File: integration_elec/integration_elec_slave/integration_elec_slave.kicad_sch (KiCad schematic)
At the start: 0 parts

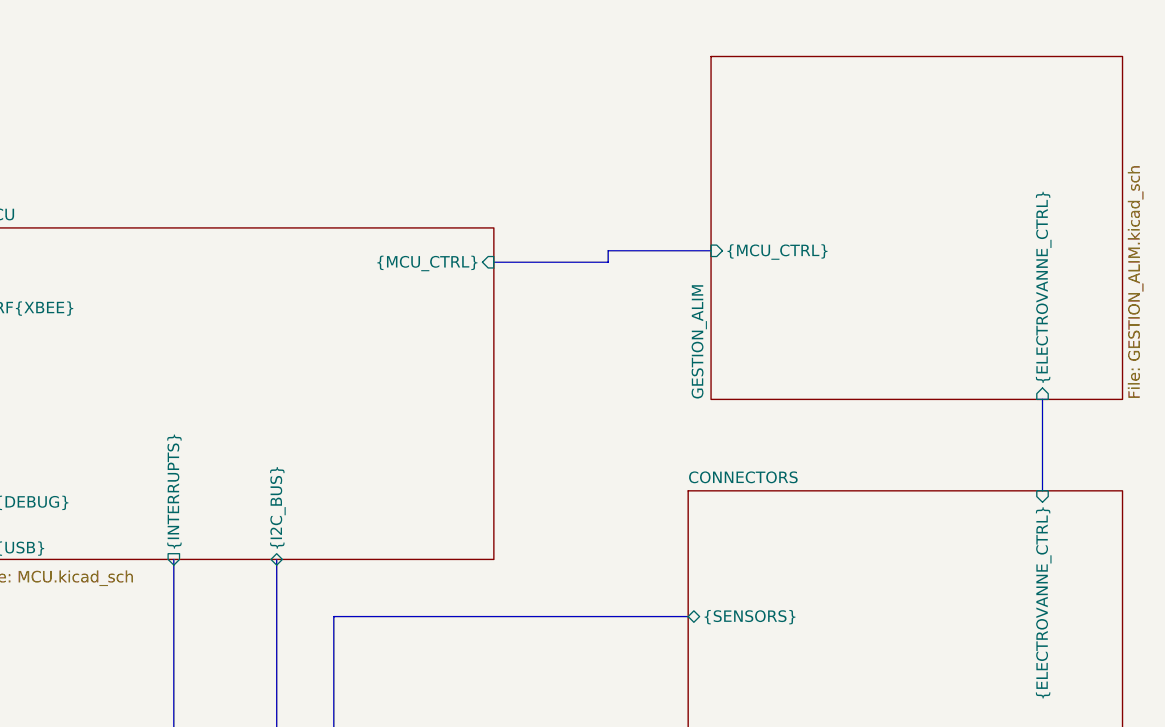
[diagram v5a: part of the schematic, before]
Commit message: EM - Fini schématique attente de review
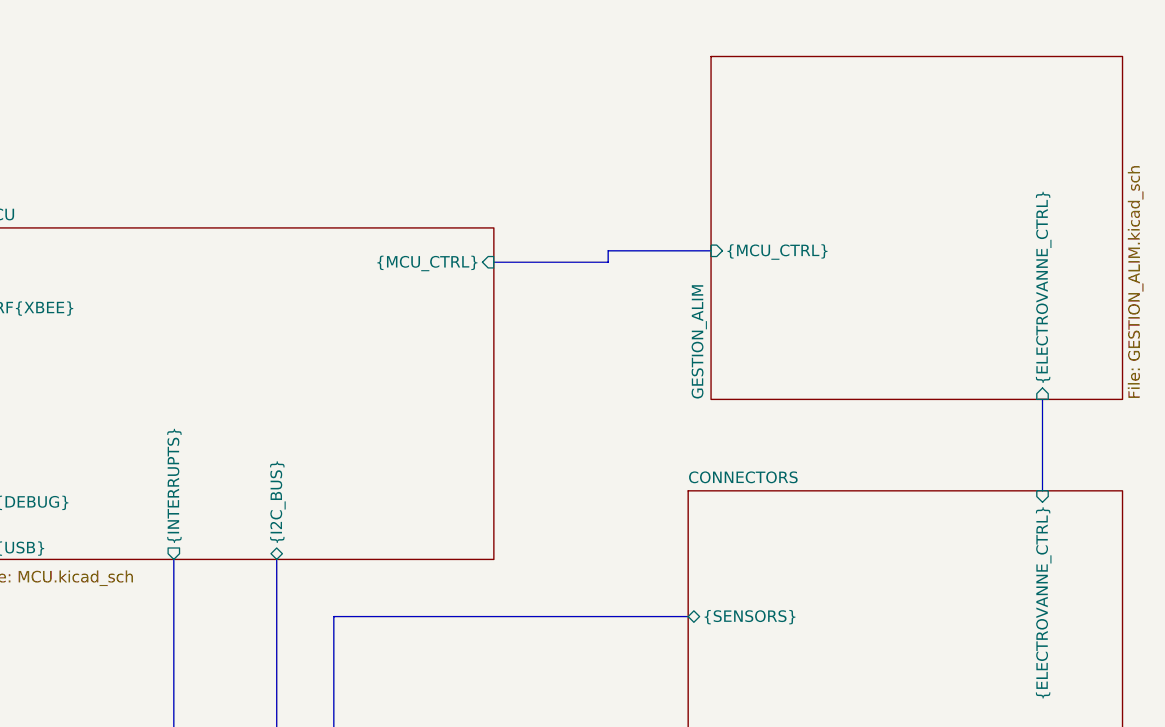
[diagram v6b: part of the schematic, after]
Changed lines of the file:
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@@
 		)
 		(pin "{ELECTROVANNE_CTRL}" input
-			(at 257.8101 81.2799 270)
+			(at 257.8101 81.28 270)
 			(effects
 				(font
@@
 		)
 		(pin "{I2C_BUS}" bidirectional
-			(at 172.72 99.695 270)
+			(at 172.72 99.06 270)
 			(effects
 				(font
@@
 		)
 		(pin "{INTERRUPTS}" output
-			(at 161.29 99.695 270)
+			(at 161.29 99.06 270)
 			(effects
 				(font

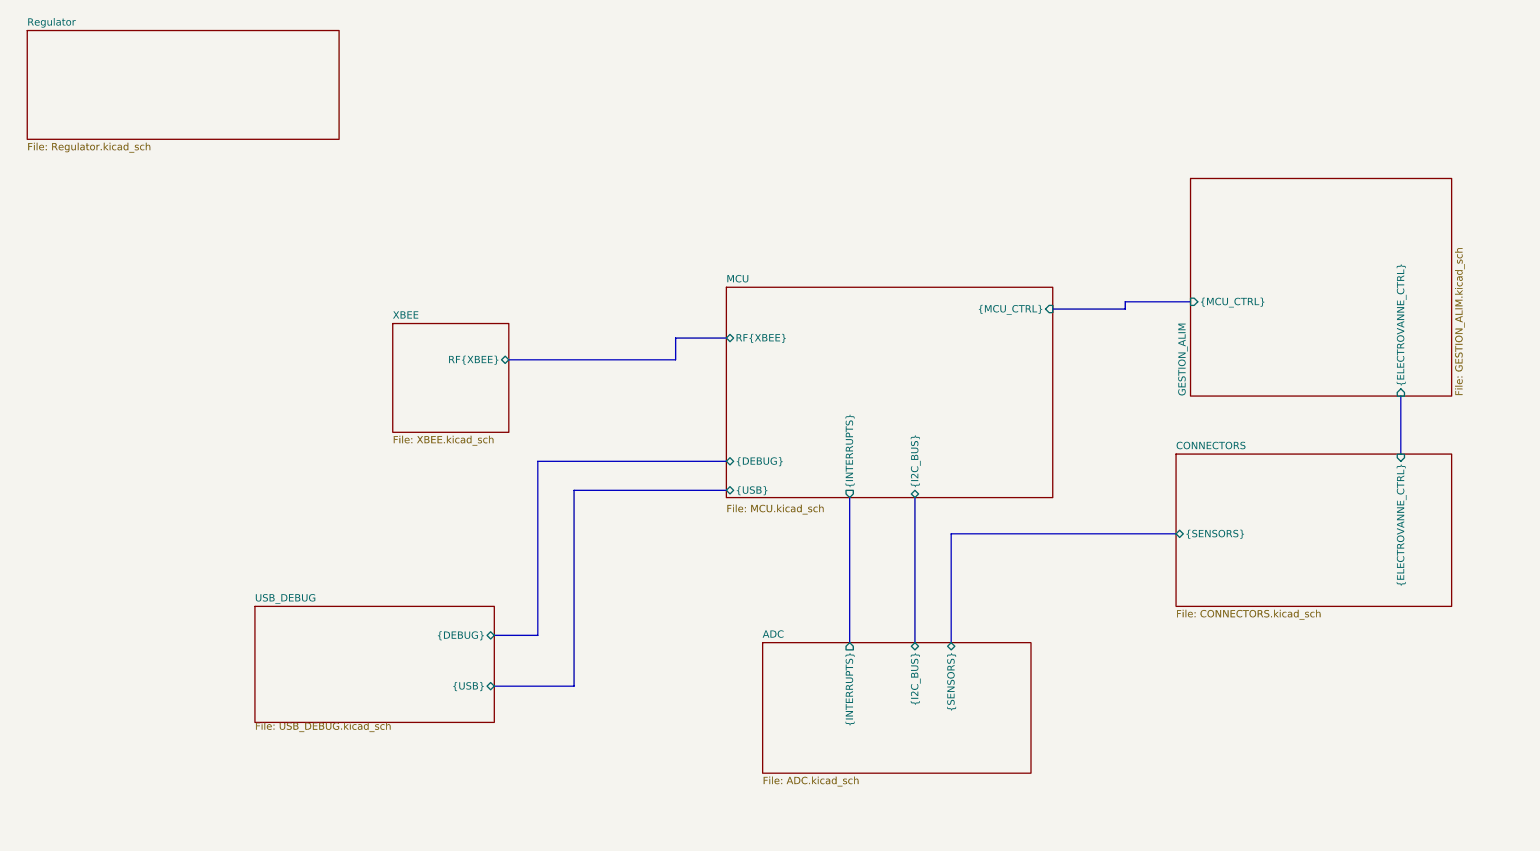
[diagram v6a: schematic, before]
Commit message: EM - Fin du schématique, ajout de diode pour empêcher de backfeeder le USB. Début PCB et ajout carré 100x100
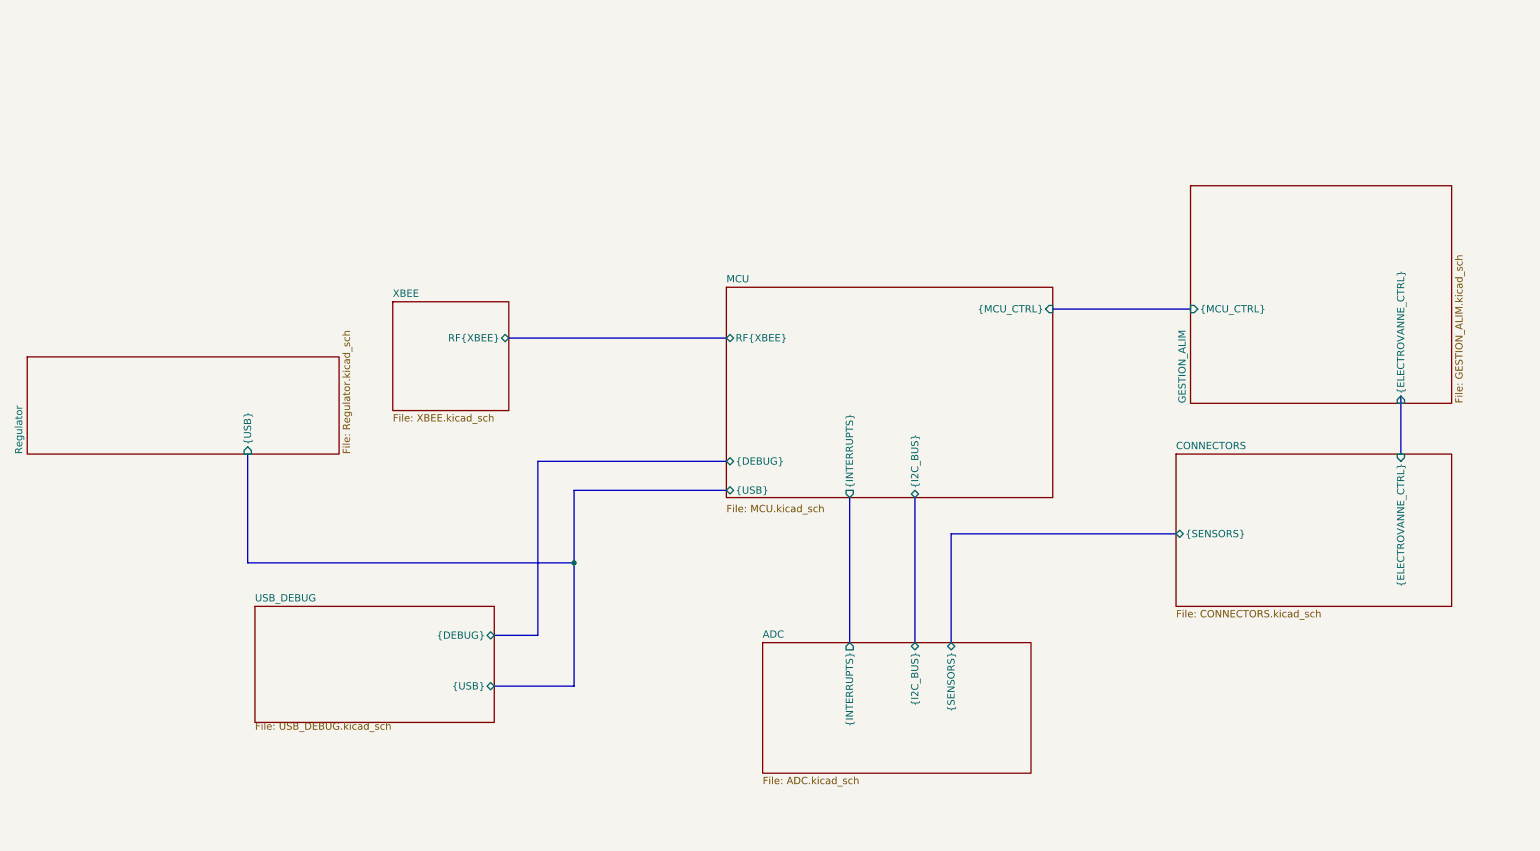
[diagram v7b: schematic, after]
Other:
- sheet Regulator ports: added {USB}; removed none
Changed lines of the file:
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@@
 	(generator_version "9.0")
 	(paper "A4")
-	(bus
-		(pts
-			(xy 209.55 66.04) (xy 209.55 64.77)
-		)
-		(stroke
-			(width 0)
-			(type default)
-		)
+	(junction
+		(at 113.03 110.49)
+		(diameter 0)
+		(color 0 0 0 0)
 	)
 	(bus
@@
 	(bus
 		(pts
-			(xy 113.03 132.08) (xy 113.03 97.79)
-		)
-		(stroke
-			(width 0)
-			(type default)
-		)
-	)
-	(bus
-		(pts
-			(xy 130.81 74.93) (xy 101.6 74.93)
+			(xy 113.03 132.08) (xy 113.03 110.49)
+		)
+		(stroke
+			(width 0)
+			(type default)
+		)
+	)
+	(bus
+		(pts
+			(xy 101.6 71.12) (xy 139.7 71.12)
+		)
+		(stroke
+			(width 0)
+			(type default)
+		)
+	)
+	(bus
+		(pts
+			(xy 113.03 110.49) (xy 113.03 97.79)
+		)
+		(stroke
+			(width 0)
+			(type default)
+		)
+	)
+	(bus
+		(pts
+			(xy 55.88 110.49) (xy 113.03 110.49)
 		)
 		(stroke
@@
 	(bus
 		(pts
-			(xy 130.81 71.12) (xy 130.81 74.93)
-		)
-		(stroke
-			(width 0)
-			(type default)
-		)
-	)
-	(bus
-		(pts
 			(xy 99.06 132.08) (xy 113.03 132.08)
 		)
@@
 	(bus
 		(pts
-			(xy 130.81 71.12) (xy 139.7 71.12)
-		)
-		(stroke
-			(width 0)
-			(type default)
-		)
-	)
-	(bus
-		(pts
 			(xy 179.07 105.41) (xy 218.44 105.41)
 		)
@@
 	(bus
 		(pts
-			(xy 209.55 64.77) (xy 220.98 64.77)
-		)
-		(stroke
-			(width 0)
-			(type default)
-		)
-	)
-	(bus
-		(pts
-			(xy 196.85 66.04) (xy 209.55 66.04)
+			(xy 55.88 91.44) (xy 55.88 110.49)
+		)
+		(stroke
+			(width 0)
+			(type default)
+		)
+	)
+	(bus
+		(pts
+			(xy 196.85 66.04) (xy 220.9799 66.04)
 		)
 		(stroke
@@
 	)
 	(sheet
-		(at 17.272 17.272)
-		(size 54.61 19.05)
+		(at 17.272 74.422)
+		(size 54.61 17.018)
 		(exclude_from_sim no)
 		(in_bom yes)
@@
 		)
 		(property "Sheetname" "Regulator"
-			(at 17.272 16.5604 0)
+			(at 16.5604 91.44 90)
 			(effects
 				(font
@@
 		)
 		(property "Sheetfile" "Regulator.kicad_sch"
-			(at 17.272 36.9066 0)
+			(at 72.4666 91.44 90)
 			(effects
 				(font
@@
 				)
 				(justify left top)
+			)
+		)
+		(pin "{USB}" input
+			(at 55.88 91.44 270)
+			(effects
+				(font
+					(size 1.27 1.27)
+				)
+				(justify left)
 			)
 		)
@@
 	)
 	(sheet
-		(at 81.28 68.58)
+		(at 81.28 64.77)
 		(size 20.32 19.05)
 		(exclude_from_sim no)
@@
 		)
 		(property "Sheetname" "XBEE"
-			(at 81.28 67.8684 0)
+			(at 81.28 64.0584 0)
 			(effects
 				(font
@@
 		)
 		(property "Sheetfile" "XBEE.kicad_sch"
-			(at 81.28 88.2146 0)
+			(at 81.28 84.4046 0)
 			(effects
 				(font
@@
 		)
 		(pin "RF{XBEE}" bidirectional
-			(at 101.6 74.93 0)
+			(at 101.6 71.12 0)
 			(effects
 				(font
@@
 	)
 	(sheet
-		(at 220.98 43.18)
+		(at 220.9799 44.45)
 		(size 45.72 38.1)
 		(exclude_from_sim no)
@@
 		)
 		(property "Sheetname" "GESTION_ALIM"
-			(at 220.2684 81.2799 90)
+			(at 220.2683 82.5499 90)
 			(effects
 				(font
@@
 		)
 		(property "Sheetfile" "GESTION_ALIM.kicad_sch"
-			(at 267.2846 81.2799 90)
+			(at 267.2845 82.5499 90)
 			(effects
 				(font
@@
 		)
 		(pin "{ELECTROVANNE_CTRL}" input
-			(at 257.8101 81.28 270)
+			(at 257.81 82.55 270)
 			(effects
 				(font
@@
 		)
 		(pin "{MCU_CTRL}" input
-			(at 220.98 64.77 180)
-			(effects
-				(font
+			(at 220.9799 66.04 180)
+			(effects
+				(font

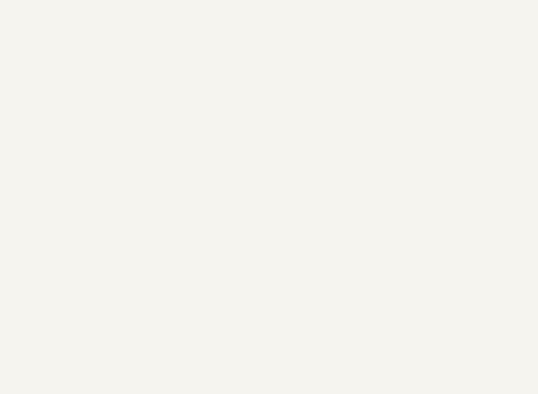
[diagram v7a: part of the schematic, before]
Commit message: EM - Avancement du placement du PCB, fini USB et RELAIS, en train de continuer micro et regulateurs
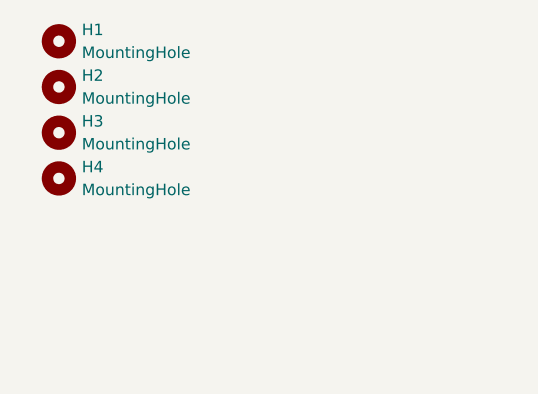
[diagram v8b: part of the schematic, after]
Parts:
- added H1, H2, H3, H4: MountingHole, MountingHole:MountingHole_3.2mm_M3, symbol Mechanical:MountingHole
